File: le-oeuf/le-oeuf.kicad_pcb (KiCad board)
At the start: 2 copper layers, 215.1 x 81.2 mm, 80 parts, among them J1 S2B-PH-K-S, SW1 PG1425, SW10 PG1425, SW11 PG1425, SW12 PG1425, SW13 PG1425, SW14 PG1425, SW15 PG1425, SW16 PG1425, SW17 PG1425, SW18 PG1425, SW19 PG1425, SW2 PG1425, SW20 PG1425, SW21 PG1425, SW22 PG1425, SW23 PG1425, SW24 PG1425, SW25 PG1425, SW26 PG1425, SW27 PG1425, SW28 PG1425, SW29 PG1425, SW3 PG1425, SW30 PG1425, SW31 PG1425, SW32 PG1425, SW33 PG1425, SW34 PG1425, SW35 PG1425, SW36 PG1425, SW37 PCM12SMTR, SW4 PG1425, SW5 PG1425, SW6 PG1425, SW7 PG1425, SW8 PG1425, SW9 PG1425, U1 Seeeduino Xiao nRF52840, U2 74HC595D,118

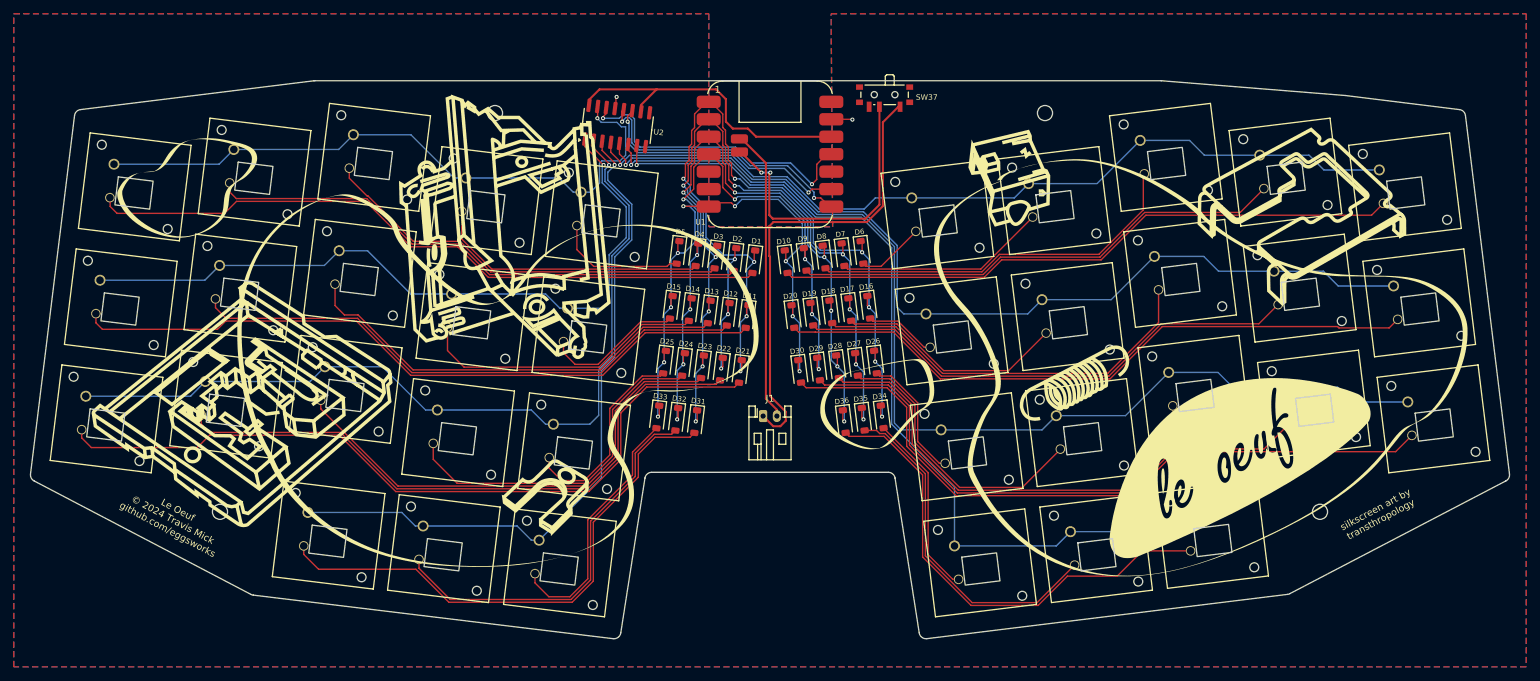
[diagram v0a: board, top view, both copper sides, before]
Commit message: added through hole to battery pads for easier hand soldering
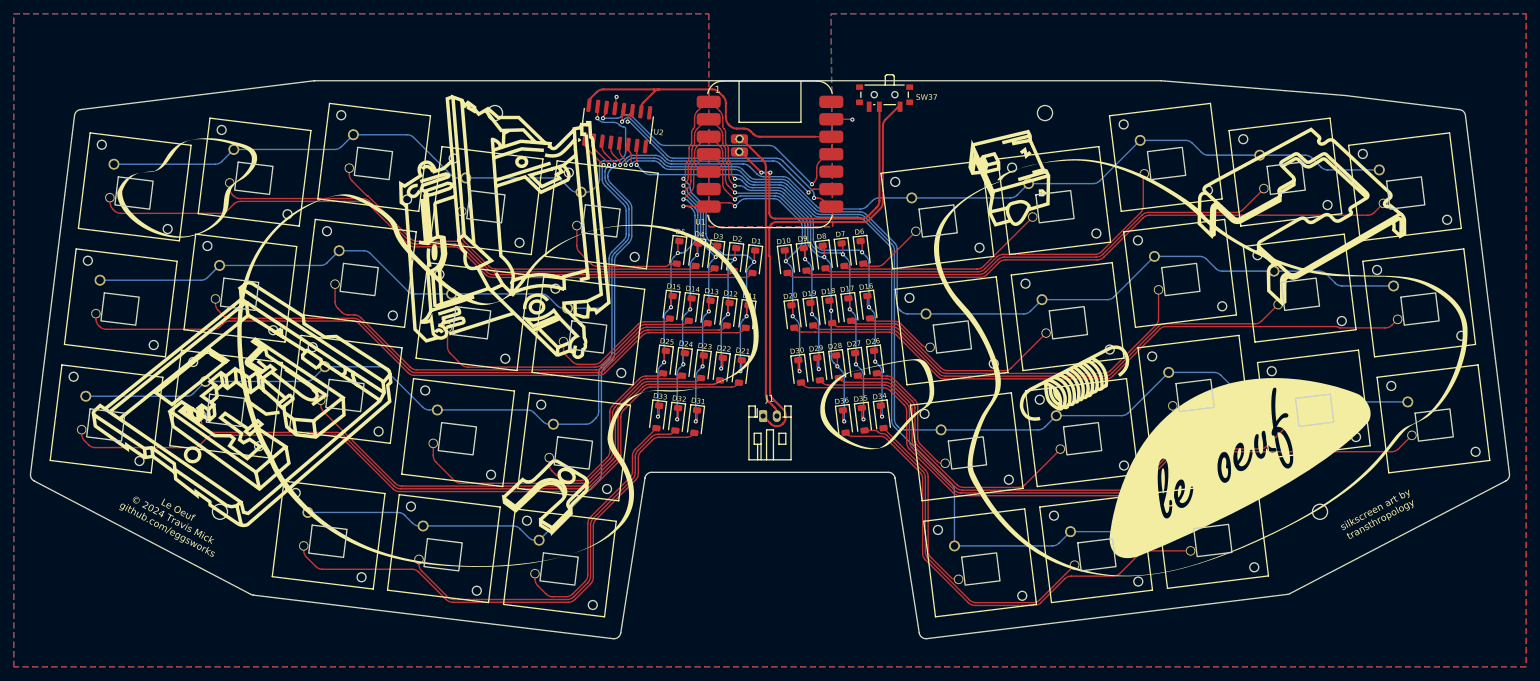
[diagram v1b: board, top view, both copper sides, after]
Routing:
- net MOSI: track 44.4 -> 42.0 mm
- net CS: track 40.6 -> 38.2 mm
- net SCK: track 37.8 -> 35.8 mm
- net C1: track 123.0 -> 121.1 mm
- net C2: track 113.3 -> 111.6 mm
- net C3: track 113.7 -> 112.3 mm
- net R7: track 152.9 -> 151.7 mm
- net R6: track 135.6 -> 134.5 mm
- net R5: track 124.0 -> 123.0 mm
- net R3: track 124.9 -> 123.8 mm
- net C5: track 89.6 -> 88.6 mm
- net R1: track 94.1 -> 93.1 mm
- net C4: track 97.3 -> 96.3 mm
- net R4: track 101.5 -> 100.7 mm
- net R2: track 107.1 -> 106.2 mm
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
